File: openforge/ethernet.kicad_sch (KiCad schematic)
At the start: 61 parts, among them P5 LPJ0011BBNL, U1 SN74AHC1G09DCKR, U14 LAN8710A, Y3 25MHz,20pF

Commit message: added footprint associations
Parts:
- R112, R113, R114, R115, R116, R117, R118, R119, R120, R121, R122, R123, R124, R125, R126, R127, R128, R129, R130, R131, R132, R133, R134, R135, R136, R137, R138, R139, R140, R141, R142, R143, R144, R145, R33, R34, R38, R39, R40, R41, R42: footprint (none) -> Resistor_SMD:R_0402_1005Metric
- U1: footprint (none) -> footprints:DCK0005A_L
- Y3: footprint (none) -> Crystal:Crystal_SMD_Abracon_ABM7-2Pin_6.0x3.5mm
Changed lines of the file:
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@@
 			)
 		)
-		(property "Footprint" ""
+		(property "Footprint" "Crystal:Crystal_SMD_Abracon_ABM7-2Pin_6.0x3.5mm"
 			(at 74.93 160.02 0)
 			(effects
@@
 			)
 		)
-		(property "Footprint" ""
+		(property "Footprint" "Resistor_SMD:R_0402_1005Metric"
 			(at 76.2 117.348 90)
 			(effects
@@
 			)
 		)
-		(property "Footprint" ""
+		(property "Footprint" "Resistor_SMD:R_0402_1005Metric"
 			(at 236.982 77.47 90)
 			(effects
@@
 			)
 		)
-		(property "Footprint" ""
+		(property "Footprint" "Resistor_SMD:R_0402_1005Metric"
 			(at 176.022 148.59 90)
 			(effects
@@
 			)
 		)
-		(property "Footprint" ""
+		(property "Footprint" "Resistor_SMD:R_0402_1005Metric"
 			(at 379.222 38.1 90)
 			(effects
@@
 			)
 		)
-		(property "Footprint" ""
+		(property "Footprint" "Resistor_SMD:R_0402_1005Metric"
 			(at 252.222 77.47 90)
 			(effects
@@
 			)
 		)
-		(property "Footprint" ""
+		(property "Footprint" "Resistor_SMD:R_0402_1005Metric"
 			(at 76.2 127.508 90)
 			(effects
@@
 			)
 		)
-		(property "Footprint" ""
+		(property "Footprint" "Resistor_SMD:R_0402_1005Metric"
 			(at 76.2 114.808 90)
 			(effects
@@
 			)
 		)
-		(property "Footprint" ""
+		(property "Footprint" "Resistor_SMD:R_0402_1005Metric"
 			(at 282.702 77.47 90)
 			(effects
@@
 			)
 		)
-		(property "Footprint" ""
+		(property "Footprint" "Resistor_SMD:R_0402_1005Metric"
 			(at 76.2 140.208 90)
 			(effects
@@
 			)
 		)
-		(property "Footprint" ""
+		(property "Footprint" "Resistor_SMD:R_0402_1005Metric"
 			(at 296.672 77.47 90)
 			(effects
@@
 			)
 		)
-		(property "Footprint" ""
+		(property "Footprint" "Resistor_SMD:R_0402_1005Metric"
 			(at 76.2 99.568 90)
 			(effects
@@
 			)
 		)
-		(property "Footprint" ""
+		(property "Footprint" "Resistor_SMD:R_0402_1005Metric"
 			(at 76.2 130.048 90)
 			(effects
@@
 			)
 		)
-		(property "Footprint" ""
+		(property "Footprint" "Resistor_SMD:R_0402_1005Metric"
 			(at 64.008 153.67 90)
 			(effects
@@
 			)
 		)
-		(property "Footprint" ""
+		(property "Footprint" "Resistor_SMD:R_0402_1005Metric"
 			(at 283.972 41.91 90)
 			(effects
@@
 			)
 		)
-		(property "Footprint" ""
+		(property "Footprint" "Resistor_SMD:R_0402_1005Metric"
 			(at 76.2 109.728 90)
 			(effects
@@
 			)
 		)
-		(property "Footprint" ""
+		(property "Footprint" "Resistor_SMD:R_0402_1005Metric"
 			(at 367.792 114.3 90)
 			(effects
@@
 			)
 		)
-		(property "Footprint" ""
+		(property "Footprint" "Resistor_SMD:R_0402_1005Metric"
 			(at 76.2 147.828 90)
 			(effects
@@
 			)
 		)
-		(property "Footprint" ""
+		(property "Footprint" "Resistor_SMD:R_0402_1005Metric"
 			(at 252.222 121.92 90)
 			(effects
@@
 			)
 		)
-		(property "Footprint" ""
+		(property "Footprint" "Resistor_SMD:R_0402_1005Metric"
 			(at 76.2 119.888 90)
 			(effects
@@
 			)
 		)
-		(property "Footprint" ""
+		(property "Footprint" "footprints:DCK0005A_L"
 			(at 148.59 227.33 0)
 			(effects
@@
 			)
 		)
-		(property "Footprint" ""
+		(property "Footprint" "Resistor_SMD:R_0402_1005Metric"
 			(at 76.2 122.428 90)
 			(effects
@@
 			)
 		)
-		(property "Footprint" ""
+		(property "Footprint" "Resistor_SMD:R_0402_1005Metric"
 			(at 117.602 71.12 90)
 			(effects
@@
 			)
 		)
-		(property "Footprint" ""
+		(property "Footprint" "Resistor_SMD:R_0402_1005Metric"
 			(at 271.272 41.91 90)
 			(effects
@@
 			)
 		)
-		(property "Footprint" ""
+		(property "Footprint" "Resistor_SMD:R_0402_1005Metric"
 			(at 76.2 97.028 90)
 			(effects
@@
 			)
 		)
-		(property "Footprint" ""
+		(property "Footprint" "Resistor_SMD:R_0402_1005Metric"
 			(at 76.2 132.588 90)
 			(effects
@@
 			)
 		)
-		(property "Footprint" ""
+		(property "Footprint" "Resistor_SMD:R_0402_1005Metric"
 			(at 377.952 114.3 90)
 			(effects
@@
 			)
 		)
-		(property "Footprint" ""
+		(property "Footprint" "Resistor_SMD:R_0402_1005Metric"
 			(at 122.682 212.09 90)
 			(effects
@@
 			)
 		)
-		(property "Footprint" ""
+		(property "Footprint" "Resistor_SMD:R_0402_1005Metric"
 			(at 76.2 102.108 90)
 			(effects
@@
 			)
 		)
-		(property "Footprint" ""
+		(property "Footprint" "Resistor_SMD:R_0402_1005Metric"
 			(at 366.522 38.1 90)
 			(effects
@@
 			)
 		)
-		(property "Footprint" ""
+		(property "Footprint" "Resistor_SMD:R_0402_1005Metric"
 			(at 76.2 94.488 90)
 			(effects
@@
 			)
 		)
-		(property "Footprint" ""
+		(property "Footprint" "Resistor_SMD:R_0402_1005Metric"
 			(at 191.262 148.59 90)
 			(effects
@@
 			)
 		)
-		(property "Footprint" ""
+		(property "Footprint" "Resistor_SMD:R_0402_1005Metric"
 			(at 267.462 77.47 90)
 			(effects
@@
 			)
 		)
-		(property "Footprint" ""
+		(property "Footprint" "Resistor_SMD:R_0402_1005Metric"
 			(at 296.672 41.91 90)
 			(effects
@@
 			)
 		)
-		(property "Footprint" ""
+		(property "Footprint" "Resistor_SMD:R_0402_1005Metric"
 			(at 184.912 213.36 90)
 			(effects
@@
 			)
 		)
-		(property "Footprint" ""
+		(property "Footprint" "Resistor_SMD:R_0402_1005Metric"
 			(at 76.2 107.188 90)
 			(effects
@@
 			)
 		)
-		(property "Footprint" ""
+		(property "Footprint" "Resistor_SMD:R_0402_1005Metric"
 			(at 76.2 89.408 90)
 			(effects
@@
 			)
 		)
-		(property "Footprint" ""
+		(property "Footprint" "Resistor_SMD:R_0402_1005Metric"
 			(at 321.31 122.682 90)
 			(effects
@@
 			)
 		)
-		(property "Footprint" ""
+		(property "Footprint" "Resistor_SMD:R_0402_1005Metric"
 			(at 76.2 112.268 90)
 			(effects
@@
 			)
 		)
-		(property "Footprint" ""
+		(property "Footprint" "Resistor_SMD:R_0402_1005Metric"
 			(at 76.2 91.948 90)
 			(effects
@@
 			)
 		)
-		(property "Footprint" ""
+		(property "Footprint" "Resistor_SMD:R_0402_1005Metric"
 			(at 258.572 41.91 90)
 			(effects
@@
 			)
 		)
-		(property "Footprint" ""
+		(property "Footprint" "Resistor_SMD:R_0402_1005Metric"
 			(at 353.822 38.1 90)
 			(effects
@@
 			)
 		)
-		(property "Footprint" ""
+		(property "Footprint" "Resistor_SMD:R_0402_1005Metric"
 			(at 110.49 147.828 90)
 			(effects

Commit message: PCB all layers copied from beaglebone black
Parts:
- P5: footprint footprints:LPJ0011BBNL_LPP -> footprints:7499010211A_WRE
- R136: footprint Resistor_SMD:R_0402_1005Metric -> Resistor_SMD:R_0805_2012Metric
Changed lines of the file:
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@@
 			)
 		)
-		(property "Footprint" "footprints:LPJ0011BBNL_LPP"
+		(property "Footprint" "footprints:7499010211A_WRE"
 			(at 304.8 90.424 0)
 			(effects
@@
 			)
 		)
-		(property "Footprint" "Resistor_SMD:R_0402_1005Metric"
+		(property "Footprint" "Resistor_SMD:R_0805_2012Metric"
 			(at 321.31 122.682 90)
 			(effects

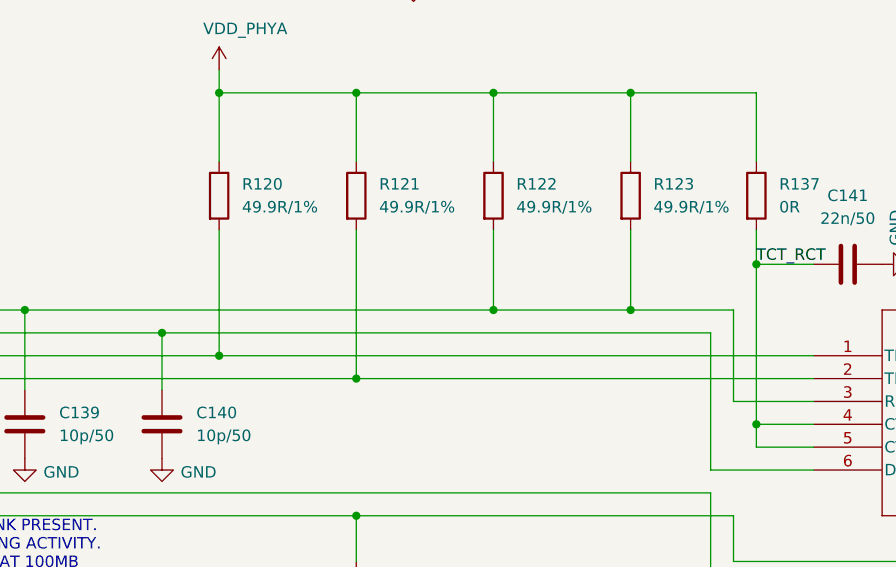
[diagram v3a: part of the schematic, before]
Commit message: fixed various footprints
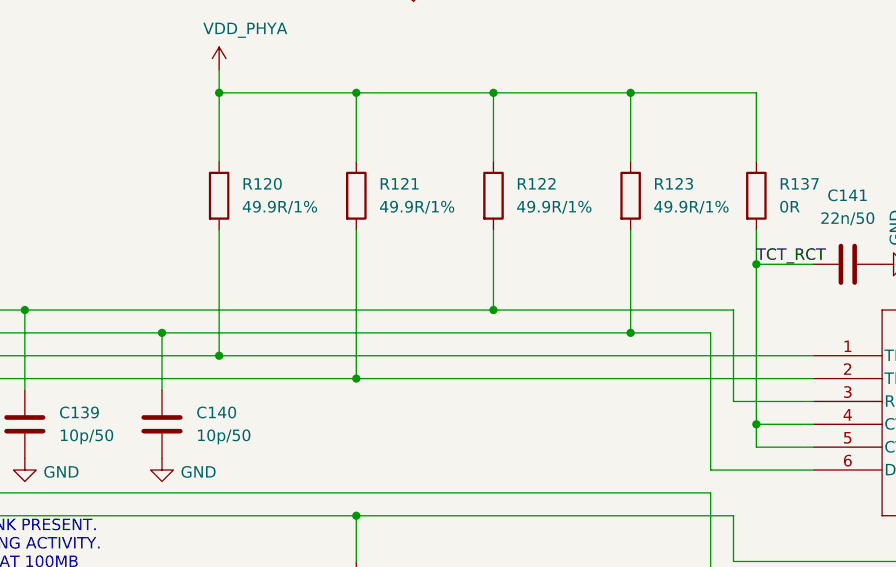
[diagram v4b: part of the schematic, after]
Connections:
- net TXN: now also R123.2
- net TXP: no longer R123.2
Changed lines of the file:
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@@
+	)
+	(junction
+		(at 284.48 92.71)
+		(diameter 0)
+		(color 0 0 0 0)
 	)
 	(junction
@@
 	)
 	(junction
-		(at 284.48 90.17)
-		(diameter 0)
-		(color 0 0 0 0)
-	)
-	(junction
 		(at 284.48 66.04)
 		(diameter 0)
@@
 	(wire
 		(pts
+			(xy 269.24 90.17) (xy 295.91 90.17)
+		)
+		(stroke
+			(width 0)
+			(type default)
+		)
+	)
+	(wire
+		(pts
 			(xy 293.37 92.71) (xy 293.37 107.95)
 		)
@@
 	(wire
 		(pts
-			(xy 232.41 92.71) (xy 293.37 92.71)
+			(xy 232.41 92.71) (xy 284.48 92.71)
 		)
 		(stroke
@@
 	(wire
 		(pts
+			(xy 284.48 92.71) (xy 293.37 92.71)
+		)
+		(stroke
+			(width 0)
+			(type default)
+		)
+	)
+	(wire
+		(pts
 			(xy 381 30.48) (xy 381 34.29)
 		)
@@
 	(wire
 		(pts
-			(xy 284.48 90.17) (xy 295.91 90.17)
-		)
-		(stroke
-			(width 0)
-			(type default)
-		)
-	)
-	(wire
-		(pts
 			(xy 97.79 43.18) (xy 97.79 46.99)
 		)
@@
 	(wire
 		(pts
-			(xy 284.48 81.28) (xy 284.48 90.17)
-		)
-		(stroke
-			(width 0)
-			(type default)
-		)
-	)
-	(wire
-		(pts
-			(xy 269.24 90.17) (xy 284.48 90.17)
-		)
-		(stroke
+			(xy 284.48 81.28) (xy 284.48 92.71)
+		)
+		(stroke

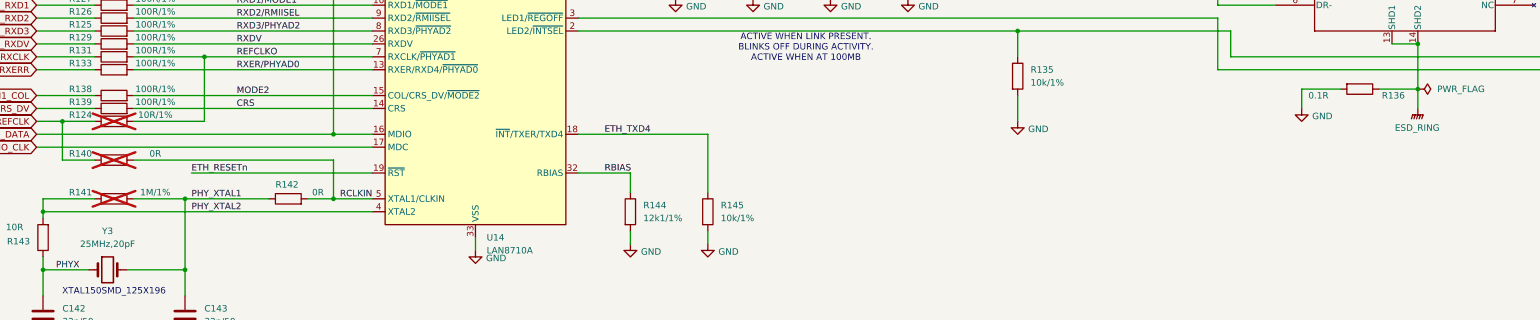
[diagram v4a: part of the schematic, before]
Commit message: fixed all errors and major warnings
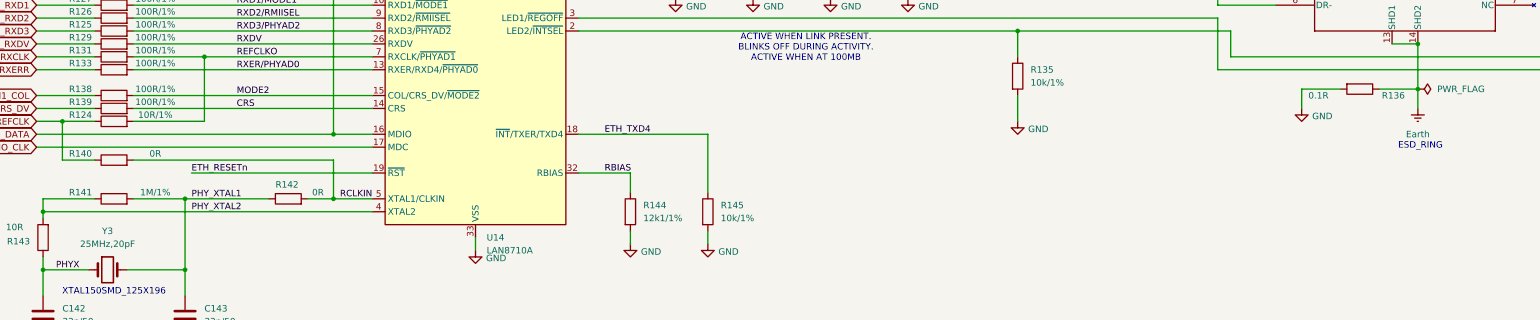
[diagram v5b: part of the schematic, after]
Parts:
- C131, C132, C134, C135, C136, C137, C138, C139, C140, C141, C142, C143, C174, C23: footprint Capacitor_SMD:C_0402_1005Metric -> footprints:C_0402_1005Metric
- C133: footprint Capacitor_SMD:C_0805_2012Metric -> footprints:C_0805_2012Metric
- R112, R113, R114, R115, R116, R117, R118, R119, R120, R121, R122, R123, R125, R126, R127, R128, R129, R130, R131, R132, R133, R134, R135, R137, R138, R139, R142, R143, R144, R145, R33, R34, R38, R39, R40, R41, R42: footprint Resistor_SMD:R_0402_1005Metric -> footprints:R_0402_1005Metric
- R124, R140, R141: footprint Resistor_SMD:R_0402_1005Metric -> footprints:R_0402_1005Metric; now fitted
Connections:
- net ESD_RING renamed Earth
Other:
- note added: "ESD_RING"
